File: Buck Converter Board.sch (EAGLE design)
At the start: 8 parts, among them J1 POWERPOLE_POWER25A_HORIZONTAL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, J2 POWERPOLE_POWER25A_HORIZONTAL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, J3 POWERPOLE_POWER25A_HORIZONTAL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

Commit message: final updates
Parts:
- D2: value 15KEXX -> (none); device diode:15KEXX -> diode:ZENER-DIODEDO34-7
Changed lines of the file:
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@@
 <grid distance="0.1" unitdist="inch" unit="inch" style="lines" multiple="1" display="no" altdistance="0.01" altunitdist="inch" altunit="inch"/>
 <layers>
-<layer number="1" name="Top" color="4" fill="1" visible="no" active="no"/>
-<layer number="2" name="Route2" color="16" fill="1" visible="no" active="no"/>
-<layer number="3" name="Route3" color="17" fill="1" visible="no" active="no"/>
-<layer number="4" name="Route4" color="18" fill="1" visible="no" active="no"/>
-<layer number="5" name="Route5" color="19" fill="1" visible="no" active="no"/>
-<layer number="6" name="Route6" color="25" fill="1" visible="no" active="no"/>
-<layer number="7" name="Route7" color="26" fill="1" visible="no" active="no"/>
-<layer number="8" name="Route8" color="27" fill="1" visible="no" active="no"/>
-<layer number="9" name="Route9" color="28" fill="1" visible="no" active="no"/>
-<layer number="10" name="Route10" color="29" fill="1" visible="no" active="no"/>
-<layer number="11" name="Route11" color="30" fill="1" visible="no" active="no"/>
-<layer number="12" name="Route12" color="20" fill="1" visible="no" active="no"/>
-<layer number="13" name="Route13" color="21" fill="1" visible="no" active="no"/>
-<layer number="14" name="Route14" color="22" fill="1" visible="no" active="no"/>
-<layer number="15" name="Route15" color="23" fill="1" visible="no" active="no"/>
-<layer number="16" name="Bottom" color="1" fill="1" visible="no" active="no"/>
-<layer number="17" name="Pads" color="2" fill="1" visible="no" active="no"/>
-<layer number="18" name="Vias" color="2" fill="1" visible="no" active="no"/>
-<layer number="19" name="Unrouted" color="6" fill="1" visible="no" active="no"/>
-<layer number="20" name="Dimension" color="24" fill="1" visible="no" active="no"/>
-<layer number="21" name="tPlace" color="7" fill="1" visible="no" active="no"/>
-<layer number="22" name="bPlace" color="7" fill="1" visible="no" active="no"/>
-<layer number="23" name="tOrigins" color="15" fill="1" visible="no" active="no"/>
-<layer number="24" name="bOrigins" color="15" fill="1" visible="no" active="no"/>
-<layer number="25" name="tNames" color="7" fill="1" visible="no" active="no"/>
-<layer number="26" name="bNames" color="7" fill="1" visible="no" active="no"/>
-<layer number="27" name="tValues" color="7" fill="1" visible="no" active="no"/>
-<layer number="28" name="bValues" color="7" fill="1" visible="no" active="no"/>
+<layer number="1" name="Top" color="4" fill="1" visible="yes" active="no"/>
+<layer number="2" name="Route2" color="16" fill="1" visible="yes" active="no"/>
+<layer number="3" name="Route3" color="17" fill="1" visible="yes" active="no"/>
+<layer number="4" name="Route4" color="18" fill="1" visible="yes" active="no"/>
+<layer number="5" name="Route5" color="19" fill="1" visible="yes" active="no"/>
+<layer number="6" name="Route6" color="25" fill="1" visible="yes" active="no"/>
+<layer number="7" name="Route7" color="26" fill="1" visible="yes" active="no"/>
+<layer number="8" name="Route8" color="27" fill="1" visible="yes" active="no"/>
+<layer number="9" name="Route9" color="28" fill="1" visible="yes" active="no"/>
+<layer number="10" name="Route10" color="29" fill="1" visible="yes" active="no"/>
+<layer number="11" name="Route11" color="30" fill="1" visible="yes" active="no"/>
+<layer number="12" name="Route12" color="20" fill="1" visible="yes" active="no"/>
+<layer number="13" name="Route13" color="21" fill="1" visible="yes" active="no"/>
+<layer number="14" name="Route14" color="22" fill="1" visible="yes" active="no"/>
+<layer number="15" name="Route15" color="23" fill="1" visible="yes" active="no"/>
+<layer number="16" name="Bottom" color="1" fill="1" visible="yes" active="no"/>
+<layer number="17" name="Pads" color="2" fill="1" visible="yes" active="no"/>
+<layer number="18" name="Vias" color="2" fill="1" visible="yes" active="no"/>
+<layer number="19" name="Unrouted" color="6" fill="1" visible="yes" active="no"/>
+<layer number="20" name="Dimension" color="24" fill="1" visible="yes" active="no"/>
+<layer number="21" name="tPlace" color="7" fill="1" visible="yes" active="no"/>
+<layer number="22" name="bPlace" color="7" fill="1" visible="yes" active="no"/>
+<layer number="23" name="tOrigins" color="15" fill="1" visible="yes" active="no"/>
+<layer number="24" name="bOrigins" color="15" fill="1" visible="yes" active="no"/>
+<layer number="25" name="tNames" color="7" fill="1" visible="yes" active="no"/>
+<layer number="26" name="bNames" color="7" fill="1" visible="yes" active="no"/>
+<layer number="27" name="tValues" color="7" fill="1" visible="yes" active="no"/>
+<layer number="28" name="bValues" color="7" fill="1" visible="yes" active="no"/>
 <layer number="29" name="tStop" color="7" fill="3" visible="no" active="no"/>
 <layer number="30" name="bStop" color="7" fill="6" visible="no" active="no"/>
@@
 <layer number="35" name="tGlue" color="7" fill="4" visible="no" active="no"/>
 <layer number="36" name="bGlue" color="7" fill="5" visible="no" active="no"/>
-<layer number="37" name="tTest" color="7" fill="1" visible="no" active="no"/>
-<layer number="38" name="bTest" color="7" fill="1" visible="no" active="no"/>
+<layer number="37" name="tTest" color="7" fill="1" visible="yes" active="no"/>
+<layer number="38" name="bTest" color="7" fill="1" visible="yes" active="no"/>
 <layer number="39" name="tKeepout" color="4" fill="11" visible="no" active="no"/>
 <layer number="40" name="bKeepout" color="1" fill="11" visible="no" active="no"/>
@@
 <layer number="44" name="Drills" color="7" fill="1" visible="no" active="no"/>
 <layer number="45" name="Holes" color="7" fill="1" visible="no" active="no"/>
-<layer number="46" name="Milling" color="3" fill="1" visible="no" active="no"/>
-<layer number="47" name="Measures" color="7" fill="1" visible="no" active="no"/>
-<layer number="48" name="Document" color="7" fill="1" visible="no" active="no"/>
-<layer number="49" name="Reference" color="7" fill="1" visible="no" active="no"/>
-<layer number="51" name="tDocu" color="7" fill="1" visible="no" active="no"/>
-<layer number="52" name="bDocu" color="7" fill="1" visible="no" active="no"/>
+<layer number="46" name="Milling" color="3" fill="1" visible="yes" active="no"/>
+<layer number="47" name="Measures" color="7" fill="1" visible="yes" active="no"/>
+<layer number="48" name="Document" color="7" fill="1" visible="yes" active="no"/>
+<layer number="49" name="Reference" color="7" fill="1" visible="yes" active="no"/>
+<layer number="51" name="tDocu" color="7" fill="1" visible="yes" active="no"/>
+<layer number="52" name="bDocu" color="7" fill="1" visible="yes" active="no"/>
 <layer number="88" name="SimResults" color="9" fill="1" visible="yes" active="yes"/>
 <layer number="89" name="SimProbes" color="9" fill="1" visible="yes" active="yes"/>
@@
 <part name="J3" library="powerpoles" deviceset="POWERPOLE_POWER" device="25A_HORIZONTAL_G2"/>
 <part name="UEE150W" library="REV Aux Circuit" deviceset="UEE150W" device=""/>
-<part name="D2" library="diode" library_urn="urn:adsk.eagle:library:210" deviceset="15KEXX" device="" package3d_urn="urn:adsk.eagle:package:43360/1"/>
+<part name="D2" library="diode" library_urn="urn:adsk.eagle:library:210" deviceset="ZENER-DIODE" device="DO34-7" package3d_urn="urn:adsk.eagle:package:43364/1"/>
 </parts>
 <sheets>
@@
 <instance part="J3" gate="G$1" x="154.94" y="81.28" smashed="yes"/>
 <instance part="UEE150W" gate="G$1" x="60.96" y="43.18" smashed="yes"/>
-<instance part="D2" gate="1" x="127" y="55.88" smashed="yes" rot="R90">
+<instance part="D2" gate="G$1" x="127" y="55.88" smashed="yes" rot="R90">
 <attribute name="NAME" x="125.095" y="53.594" size="1.778" layer="95" rot="R90"/>
 <attribute name="VALUE" x="130.429" y="53.594" size="1.778" layer="96" rot="R90"/>
@@
 <wire x1="127" y1="58.42" x2="127" y2="66.04" width="0.1524" layer="91"/>
 <junction x="127" y="66.04"/>
-<pinref part="D2" gate="1" pin="C"/>
+<pinref part="D2" gate="G$1" pin="C"/>
 <pinref part="UEE150W" gate="G$1" pin="SENSE+"/>
 <wire x1="101.6" y1="60.96" x2="106.68" y2="60.96" width="0.1524" layer="91"/>
@@
 <segment>
 <wire x1="127" y1="48.26" x2="127" y2="53.34" width="0.1524" layer="91"/>
-<pinref part="D2" gate="1" pin="A"/>
+<pinref part="D2" gate="G$1" pin="A"/>
 <pinref part="C1" gate="G$1" pin="2"/>
 <wire x1="114.3" y1="50.8" x2="114.3" y2="45.72" width="0.1524" layer="91"/>

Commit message: changed buck board
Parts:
- removed J1: POWERPOLE_POWER25A_HORIZONTAL_G2, powerpoles:POWERPOLE_POWER25A_HORIZONTAL_G2
- added BGND, VBATT: VBATT, master_library:TEST_POINTSPAD1-13Y
- added BUCK_GND, BUCK_OUT: TEST_POINTSPAD1-13Y, master_library:TEST_POINTSPAD1-13Y
- added U$1: BATTERY, master_library:BATTERY
- D1: value (none) -> 15V
- renumbered D2 to D1
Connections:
- net BGND: now also BGND.TP, U$1.-; no longer J1.GND
- net OGND: now also BUCK_GND.TP
- net VBATT: now also U$1.+, VBATT.TP; no longer J1.V+
- net V_OUT: now also BUCK_OUT.TP

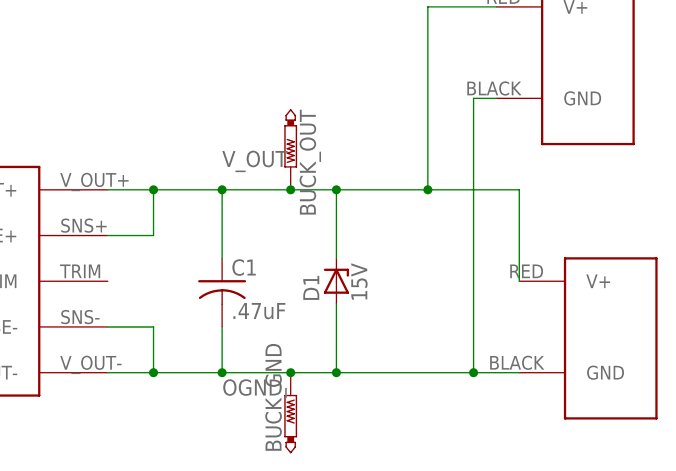
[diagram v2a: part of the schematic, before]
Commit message: changed boards, added LEDs
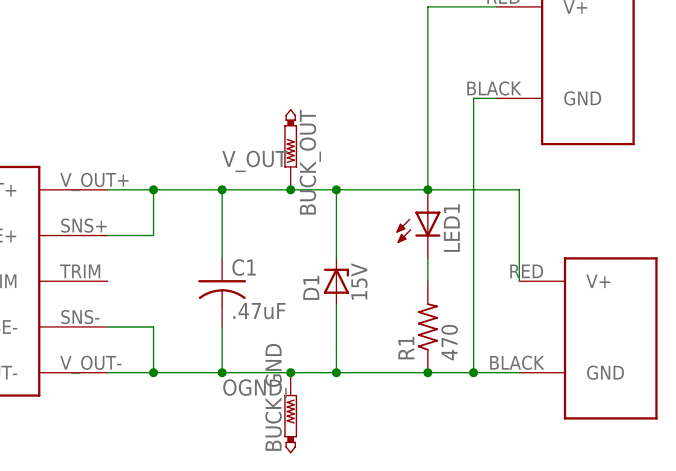
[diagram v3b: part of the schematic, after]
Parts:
- added LED1: (no value), led:LEDCHIP-LED0805
- added R1: 470, master_library:R-US_M0805
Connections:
- new net N$1: LED1.C, R1.2
- net OGND: now also R1.1
- net V_OUT: now also LED1.A
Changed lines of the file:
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@@
 <grid distance="0.1" unitdist="inch" unit="inch" style="lines" multiple="1" display="no" altdistance="0.01" altunitdist="inch" altunit="inch"/>
 <layers>
-<layer number="1" name="Top" color="4" fill="1" visible="yes" active="no"/>
-<layer number="2" name="Route2" color="16" fill="1" visible="yes" active="no"/>
-<layer number="3" name="Route3" color="17" fill="1" visible="yes" active="no"/>
-<layer number="4" name="Route4" color="18" fill="1" visible="yes" active="no"/>
-<layer number="5" name="Route5" color="19" fill="1" visible="yes" active="no"/>
-<layer number="6" name="Route6" color="25" fill="1" visible="yes" active="no"/>
-<layer number="7" name="Route7" color="26" fill="1" visible="yes" active="no"/>
-<layer number="8" name="Route8" color="27" fill="1" visible="yes" active="no"/>
-<layer number="9" name="Route9" color="28" fill="1" visible="yes" active="no"/>
-<layer number="10" name="Route10" color="29" fill="1" visible="yes" active="no"/>
-<layer number="11" name="Route11" color="30" fill="1" visible="yes" active="no"/>
-<layer number="12" name="Route12" color="20" fill="1" visible="yes" active="no"/>
-<layer number="13" name="Route13" color="21" fill="1" visible="yes" active="no"/>
-<layer number="14" name="Route14" color="22" fill="1" visible="yes" active="no"/>
-<layer number="15" name="Route15" color="23" fill="1" visible="yes" active="no"/>
-<layer number="16" name="Bottom" color="1" fill="1" visible="yes" active="no"/>
-<layer number="17" name="Pads" color="2" fill="1" visible="yes" active="no"/>
-<layer number="18" name="Vias" color="2" fill="1" visible="yes" active="no"/>
-<layer number="19" name="Unrouted" color="6" fill="1" visible="yes" active="no"/>
-<layer number="20" name="Dimension" color="24" fill="1" visible="yes" active="no"/>
-<layer number="21" name="tPlace" color="7" fill="1" visible="yes" active="no"/>
-<layer number="22" name="bPlace" color="7" fill="1" visible="yes" active="no"/>
-<layer number="23" name="tOrigins" color="15" fill="1" visible="yes" active="no"/>
-<layer number="24" name="bOrigins" color="15" fill="1" visible="yes" active="no"/>
-<layer number="25" name="tNames" color="7" fill="1" visible="yes" active="no"/>
-<layer number="26" name="bNames" color="7" fill="1" visible="yes" active="no"/>
-<layer number="27" name="tValues" color="7" fill="1" visible="yes" active="no"/>
-<layer number="28" name="bValues" color="7" fill="1" visible="yes" active="no"/>
+<layer number="1" name="Top" color="4" fill="1" visible="no" active="no"/>
+<layer number="2" name="Route2" color="16" fill="1" visible="no" active="no"/>
+<layer number="3" name="Route3" color="17" fill="1" visible="no" active="no"/>
+<layer number="4" name="Route4" color="18" fill="1" visible="no" active="no"/>
+<layer number="5" name="Route5" color="19" fill="1" visible="no" active="no"/>
+<layer number="6" name="Route6" color="25" fill="1" visible="no" active="no"/>
+<layer number="7" name="Route7" color="26" fill="1" visible="no" active="no"/>
+<layer number="8" name="Route8" color="27" fill="1" visible="no" active="no"/>
+<layer number="9" name="Route9" color="28" fill="1" visible="no" active="no"/>
+<layer number="10" name="Route10" color="29" fill="1" visible="no" active="no"/>
+<layer number="11" name="Route11" color="30" fill="1" visible="no" active="no"/>
+<layer number="12" name="Route12" color="20" fill="1" visible="no" active="no"/>
+<layer number="13" name="Route13" color="21" fill="1" visible="no" active="no"/>
+<layer number="14" name="Route14" color="22" fill="1" visible="no" active="no"/>
+<layer number="15" name="Route15" color="23" fill="1" visible="no" active="no"/>
+<layer number="16" name="Bottom" color="1" fill="1" visible="no" active="no"/>
+<layer number="17" name="Pads" color="2" fill="1" visible="no" active="no"/>
+<layer number="18" name="Vias" color="2" fill="1" visible="no" active="no"/>
+<layer number="19" name="Unrouted" color="6" fill="1" visible="no" active="no"/>
+<layer number="20" name="Dimension" color="24" fill="1" visible="no" active="no"/>
+<layer number="21" name="tPlace" color="7" fill="1" visible="no" active="no"/>
+<layer number="22" name="bPlace" color="7" fill="1" visible="no" active="no"/>
+<layer number="23" name="tOrigins" color="15" fill="1" visible="no" active="no"/>
+<layer number="24" name="bOrigins" color="15" fill="1" visible="no" active="no"/>
+<layer number="25" name="tNames" color="7" fill="1" visible="no" active="no"/>
+<layer number="26" name="bNames" color="7" fill="1" visible="no" active="no"/>
+<layer number="27" name="tValues" color="7" fill="1" visible="no" active="no"/>
+<layer number="28" name="bValues" color="7" fill="1" visible="no" active="no"/>
 <layer number="29" name="tStop" color="7" fill="3" visible="no" active="no"/>
 <layer number="30" name="bStop" color="7" fill="6" visible="no" active="no"/>
@@
 <layer number="35" name="tGlue" color="7" fill="4" visible="no" active="no"/>
 <layer number="36" name="bGlue" color="7" fill="5" visible="no" active="no"/>
-<layer number="37" name="tTest" color="7" fill="1" visible="yes" active="no"/>
-<layer number="38" name="bTest" color="7" fill="1" visible="yes" active="no"/>
+<layer number="37" name="tTest" color="7" fill="1" visible="no" active="no"/>
+<layer number="38" name="bTest" color="7" fill="1" visible="no" active="no"/>
 <layer number="39" name="tKeepout" color="4" fill="11" visible="no" active="no"/>
 <layer number="40" name="bKeepout" color="1" fill="11" visible="no" active="no"/>
@@
 <layer number="44" name="Drills" color="7" fill="1" visible="no" active="no"/>
 <layer number="45" name="Holes" color="7" fill="1" visible="no" active="no"/>
-<layer number="46" name="Milling" color="3" fill="1" visible="yes" active="no"/>
-<layer number="47" name="Measures" color="7" fill="1" visible="yes" active="no"/>
-<layer number="48" name="Document" color="7" fill="1" visible="yes" active="no"/>
-<layer number="49" name="Reference" color="7" fill="1" visible="yes" active="no"/>
-<layer number="50" name="dxf" color="7" fill="1" visible="yes" active="no"/>
-<layer number="51" name="tDocu" color="7" fill="1" visible="yes" active="no"/>
-<layer number="52" name="bDocu" color="7" fill="1" visible="yes" active="no"/>
-<layer number="53" name="tGND_GNDA" color="7" fill="1" visible="yes" active="no"/>
-<layer number="54" name="bGND_GNDA" color="7" fill="1" visible="yes" active="no"/>
-<layer number="56" name="wert" color="7" fill="1" visible="yes" active="no"/>
-<layer number="57" name="tCAD" color="7" fill="1" visible="yes" active="no"/>
-<layer number="59" name="tCarbon" color="7" fill="1" visible="yes" active="no"/>
-<layer number="60" name="bCarbon" color="7" fill="1" visible="yes" active="no"/>
+<layer number="46" name="Milling" color="3" fill="1" visible="no" active="no"/>
+<layer number="47" name="Measures" color="7" fill="1" visible="no" active="no"/>
+<layer number="48" name="Document" color="7" fill="1" visible="no" active="no"/>
+<layer number="49" name="Reference" color="7" fill="1" visible="no" active="no"/>
+<layer number="50" name="dxf" color="7" fill="1" visible="no" active="no"/>
+<layer number="51" name="tDocu" color="7" fill="1" visible="no" active="no"/>
+<layer number="52" name="bDocu" color="7" fill="1" visible="no" active="no"/>
+<layer number="53" name="tGND_GNDA" color="7" fill="1" visible="no" active="no"/>
+<layer number="54" name="bGND_GNDA" color="7" fill="1" visible="no" active="no"/>
+<layer number="56" name="wert" color="7" fill="1" visible="no" active="no"/>
+<layer number="57" name="tCAD" color="7" fill="1" visible="no" active="no"/>
+<layer number="59" name="tCarbon" color="7" fill="1" visible="no" active="no"/>
+<layer number="60" name="bCarbon" color="7" fill="1" visible="no" active="no"/>
 <layer number="88" name="SimResults" color="9" fill="1" visible="yes" active="yes"/>
 <layer number="89" name="SimProbes" color="9" fill="1" visible="yes" active="yes"/>
@@
 <part name="BUCK_GND" library="master_library" deviceset="TEST_POINTS" device="PAD1-13Y" package3d_urn="urn:adsk.eagle:package:2274087/1"/>
 <part name="BGND" library="master_library" deviceset="TEST_POINTS" device="PAD1-13Y" package3d_urn="urn:adsk.eagle:package:2274087/1" value="VBATT"/>
+<part name="LED1" library="led" library_urn="urn:adsk.eagle:library:259" deviceset="LED" device="CHIP-LED0805" package3d_urn="urn:adsk.eagle:package:15818/2"/>
+<part name="R1" library="master_library" deviceset="R-US_" device="M0805" package3d_urn="urn:adsk.eagle:package:2274058/1" value="470"/>
 </parts>
 <sheets>
@@
 <instance part="BUCK_GND" gate="G$1" x="121.92" y="43.18"/>
 <instance part="BGND" gate="G$1" x="22.86" y="53.34"/>
+<instance part="LED1" gate="G$1" x="137.16" y="63.5"/>
+<instance part="R1" gate="G$1" x="137.16" y="50.8" rot="R90"/>
 </instances>
 <busses>
@@
 <pinref part="BUCK_OUT" gate="G$1" pin="TP"/>
 <junction x="121.92" y="66.04"/>
+<pinref part="LED1" gate="G$1" pin="A"/>
 </segment>
 </net>
@@
 <pinref part="J2" gate="G$1" pin="GND"/>
 <wire x1="147.32" y1="45.72" x2="142.24" y2="45.72" width="0.1524" layer="91"/>
-<wire x1="142.24" y1="45.72" x2="127" y2="45.72" width="0.1524" layer="91"/>
+<wire x1="142.24" y1="45.72" x2="137.16" y2="45.72" width="0.1524" layer="91"/>
+<wire x1="137.16" y1="45.72" x2="127" y2="45.72" width="0.1524" layer="91"/>
 <wire x1="127" y1="45.72" x2="121.92" y2="45.72" width="0.1524" layer="91"/>
 <wire x1="121.92" y1="45.72" x2="114.3" y2="45.72" width="0.1524" layer="91"/>
@@
 <pinref part="BUCK_GND" gate="G$1" pin="TP"/>
 <junction x="121.92" y="45.72"/>
-</segment>
-</net>
+<pinref part="R1" gate="G$1" pin="1"/>
+<junction x="137.16" y="45.72"/>
+</segment>
+</net>
+<net name="N$1" class="0">
+<segment>
+<pinref part="LED1" gate="G$1" pin="C"/>
+<pinref part="R1" gate="G$1" pin="2"/>
+<wire x1="137.16" y1="55.88" x2="137.16" y2="58.42" width="0.1524" layer="91"/>
+</segment>
+</net>

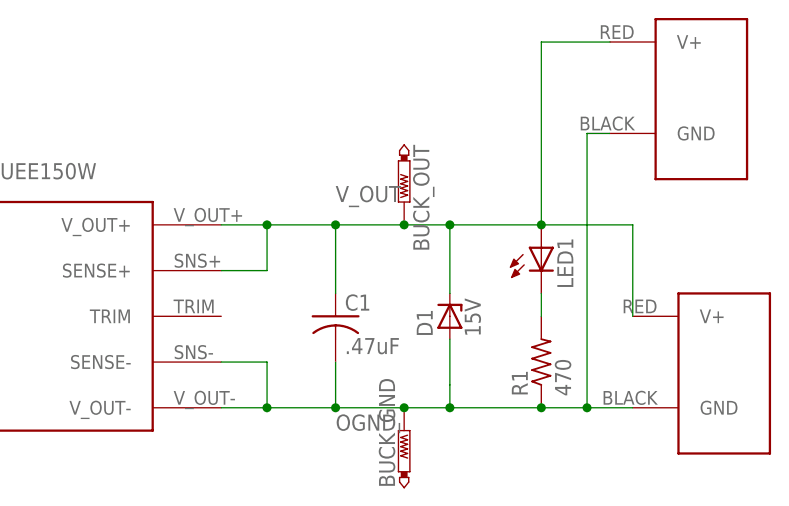
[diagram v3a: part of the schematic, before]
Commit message: changed bypass cap on 555 to 22uF panasonic
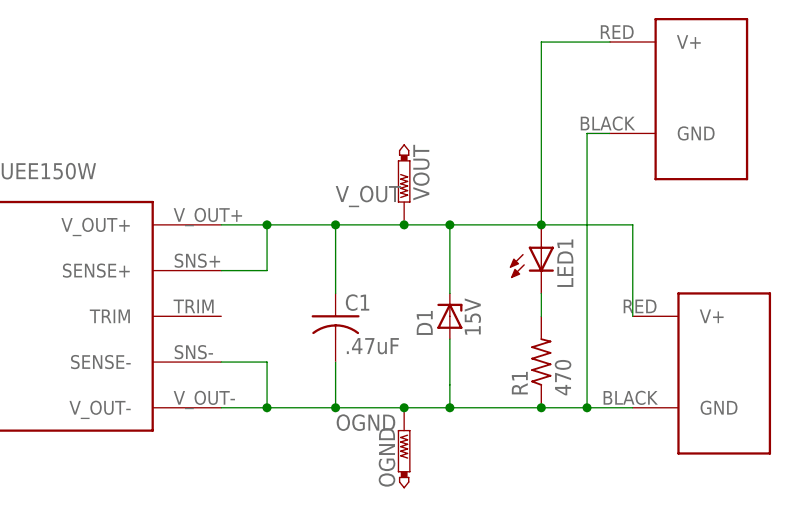
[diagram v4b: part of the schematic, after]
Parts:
- R1: device master_library:R-US_M0805 -> master_library:R-US_R3225
- renumbered BUCK_GND to OGND, BUCK_OUT to VOUT
